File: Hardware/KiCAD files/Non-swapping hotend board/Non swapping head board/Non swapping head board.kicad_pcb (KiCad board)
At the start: 2 copper layers, 21.6 x 31.7 mm, 4 parts, among them J1 JST_06, J18 JST_1mm_3_Vertical, J20 PINHD_1x10_Female, J22 Conn_01x02

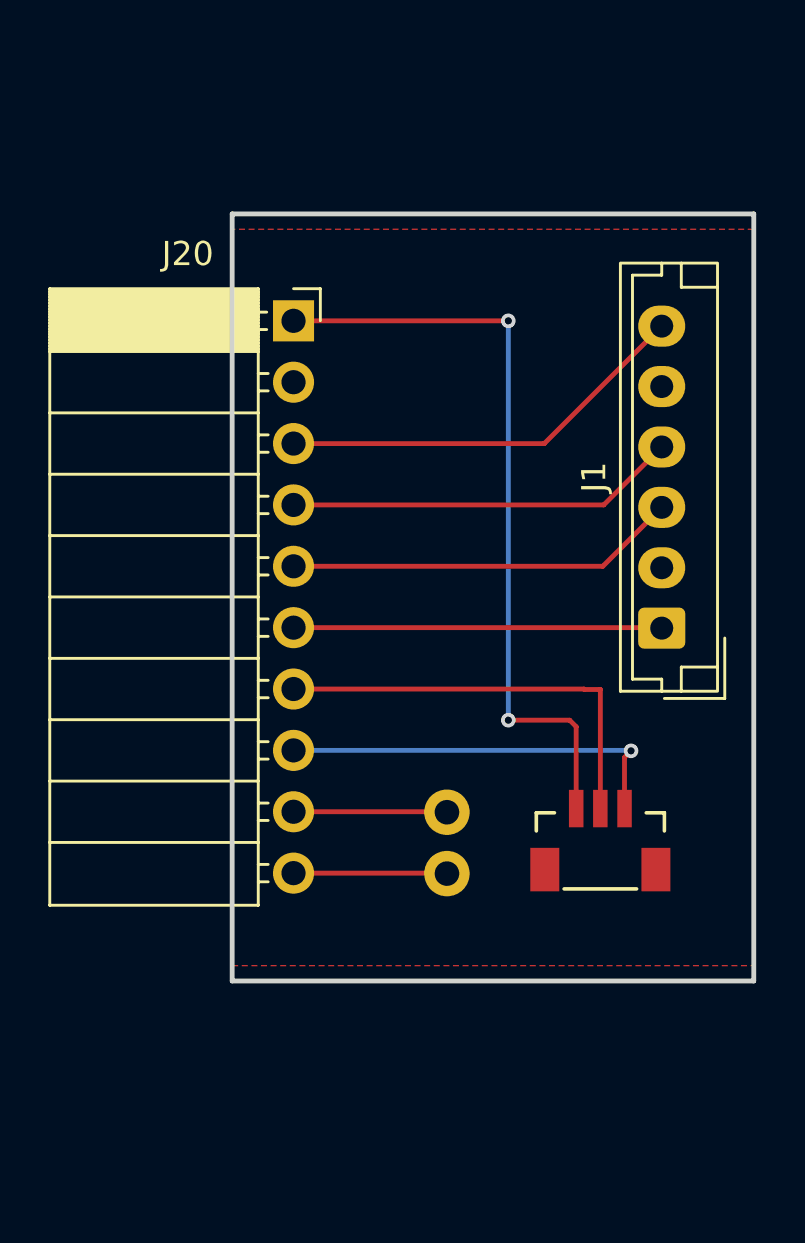
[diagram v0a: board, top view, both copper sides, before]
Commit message: 1st push of PCB's for printing
This is pre-peer review. This almost certainly has section that need adjustment. also realized I'm missing the USB-Uart bridge. first thing added in next version.
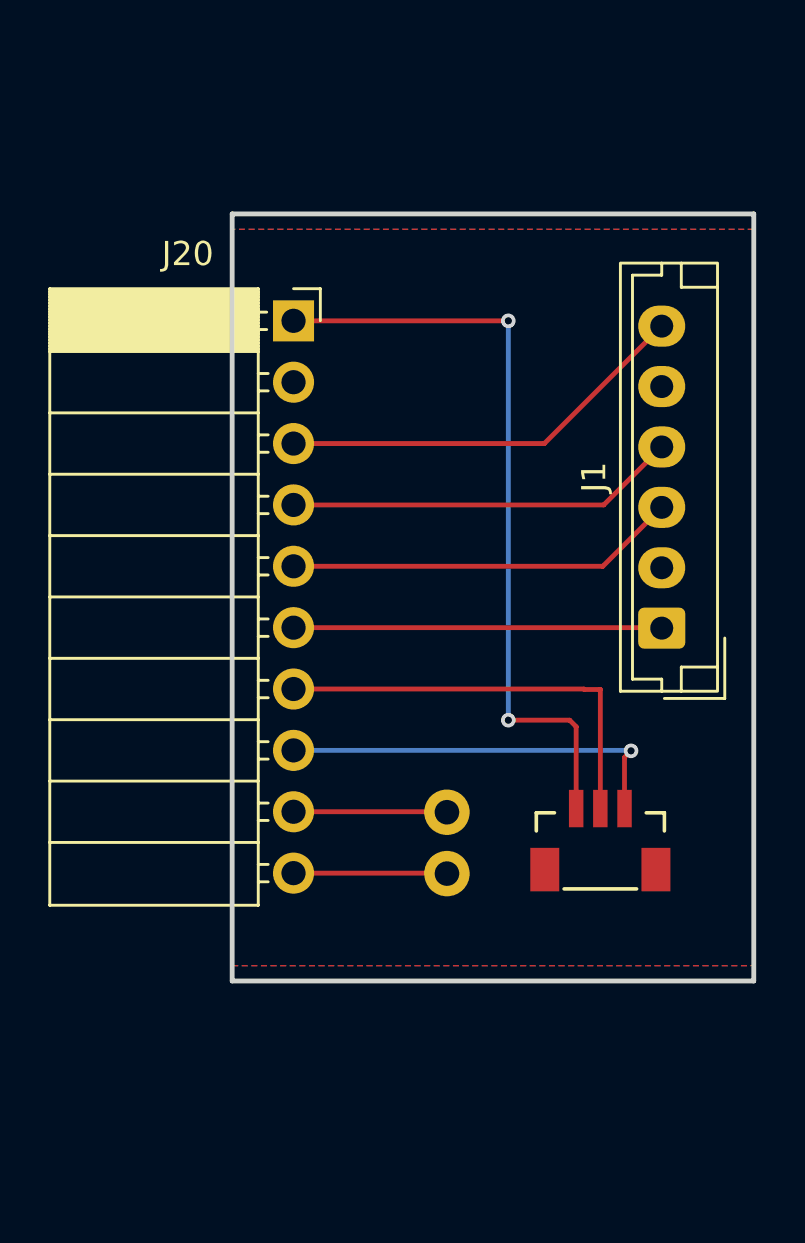
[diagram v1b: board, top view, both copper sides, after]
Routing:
- added copper zone on B.Cu, net GND
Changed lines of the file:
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@@
+	)
+	(segment
+		(start 109.49 61.23)
+		(end 109.22 60.96)
+		(width 0.2)
+		(layer "F.Cu")
+		(net "Net-(J18-Pad3)")
+	)
+	(segment
+		(start 109.22 60.96)
+		(end 106.68 60.96)
+		(width 0.2)
+		(layer "F.Cu")
+		(net "Net-(J18-Pad3)")
+	)
+	(segment
+		(start 106.68 44.43)
+		(end 97.79 44.43)
+		(width 0.2)
+		(layer "F.Cu")
+		(net "Net-(J18-Pad3)")
+	)
+	(segment
+		(start 109.49 64.6185)
+		(end 109.49 61.23)
+		(width 0.2)
+		(layer "F.Cu")
+		(net "Net-(J18-Pad3)")
+	)
+	(via
+		(at 106.68 60.96)
+		(size 0.6)
+		(drill 0.3)
+		(layers "F.Cu" "B.Cu")
+		(net "Net-(J18-Pad3)")
+	)
+	(via
+		(at 106.68 44.43)
+		(size 0.6)
+		(drill 0.3)
+		(layers "F.Cu" "B.Cu")
+		(net "Net-(J18-Pad3)")
+	)
+	(segment
+		(start 106.68 44.43)
+		(end 106.68 60.96)
+		(width 0.2)
+		(layer "B.Cu")
+		(net "Net-(J18-Pad3)")
+	)
+	(segment
+		(start 108.17 49.51)
+		(end 97.79 49.51)
+		(width 0.2)
+		(layer "F.Cu")
+		(net "/A1")
+	)
+	(segment
+		(start 113.03 44.65)
+		(end 108.17 49.51)
+		(width 0.2)
+		(layer "F.Cu")
+		(net "/A1")
+	)
+	(segment
+		(start 113.03 49.65)
+		(end 110.63 52.05)
+		(width 0.2)
+		(layer "F.Cu")
+		(net "/B1")
+	)
+	(segment
+		(start 110.63 52.05)
+		(end 97.79 52.05)
+		(width 0.2)
+		(layer "F.Cu")
+		(net "/B1")
+	)
+	(segment
+		(start 110.59 54.59)
+		(end 97.79 54.59)
+		(width 0.2)
+		(layer "F.Cu")
+		(net "/A2")
+	)
+	(segment
+		(start 113.03 52.15)
+		(end 110.59 54.59)
+		(width 0.2)
+		(layer "F.Cu")
+		(net "/A2")
+	)
+	(segment
+		(start 113.01 57.13)
+		(end 97.79 57.13)
+		(width 0.2)
+		(layer "F.Cu")
+		(net "/B2")
+	)
+	(segment
+		(start 113.03 57.15)
+		(end 113.01 57.13)
+		(width 0.2)
+		(layer "F.Cu")
+		(net "/B2")
+	)
+	(segment
+		(start 110.49 59.69)
+		(end 109.83 59.69)
+		(width 0.2)
+		(layer "F.Cu")
+		(net "Net-(J18-Pad2)")
+	)
+	(segment
+		(start 109.83 59.69)
+		(end 109.81 59.67)
+		(width 0.2)
+		(layer "F.Cu")
+		(net "Net-(J18-Pad2)")
+	)
+	(segment
+		(start 109.81 59.67)
+		(end 97.79 59.67)
+		(width 0.2)
+		(layer "F.Cu")
+		(net "Net-(J18-Pad2)")
+	)
+	(segment
+		(start 110.49 64.6185)
+		(end 110.49 59.69)
+		(width 0.2)
+		(layer "F.Cu")
+		(net "Net-(J18-Pad2)")
 	)
 	(segment
@@
 	)
 	(segment
-		(start 109.49 61.23)
-		(end 109.22 60.96)
-		(width 0.2)
-		(layer "F.Cu")
-		(net "Net-(J18-Pad3)")
-	)
-	(segment
-		(start 109.22 60.96)
-		(end 106.68 60.96)
-		(width 0.2)
-		(layer "F.Cu")
-		(net "Net-(J18-Pad3)")
-	)
-	(segment
-		(start 106.68 44.43)
-		(end 97.79 44.43)
-		(width 0.2)
-		(layer "F.Cu")
-		(net "Net-(J18-Pad3)")
-	)
-	(segment
-		(start 109.49 64.6185)
-		(end 109.49 61.23)
-		(width 0.2)
-		(layer "F.Cu")
-		(net "Net-(J18-Pad3)")
-	)
-	(via
-		(at 106.68 60.96)
-		(size 0.6)
-		(drill 0.3)
-		(layers "F.Cu" "B.Cu")
-		(net "Net-(J18-Pad3)")
-	)
-	(via
-		(at 106.68 44.43)
-		(size 0.6)
-		(drill 0.3)
-		(layers "F.Cu" "B.Cu")
-		(net "Net-(J18-Pad3)")
-	)
-	(segment
-		(start 106.68 44.43)
-		(end 106.68 60.96)
-		(width 0.2)
-		(layer "B.Cu")
-		(net "Net-(J18-Pad3)")
-	)
-	(segment
-		(start 110.49 59.69)
-		(end 109.83 59.69)
-		(width 0.2)
-		(layer "F.Cu")
-		(net "Net-(J18-Pad2)")
-	)
-	(segment
-		(start 109.83 59.69)
-		(end 109.81 59.67)
-		(width 0.2)
-		(layer "F.Cu")
-		(net "Net-(J18-Pad2)")
-	)
-	(segment
-		(start 109.81 59.67)
-		(end 97.79 59.67)
-		(width 0.2)
-		(layer "F.Cu")
-		(net "Net-(J18-Pad2)")
-	)
-	(segment
-		(start 110.49 64.6185)
-		(end 110.49 59.69)
-		(width 0.2)
-		(layer "F.Cu")
-		(net "Net-(J18-Pad2)")
-	)
-	(segment
 		(start 104.14 64.77)
 		(end 104.12 64.75)
@@
 		(net "Net-(J22-Pin_1)")
 	)
-	(segment
-		(start 113.01 57.13)
-		(end 97.79 57.13)
-		(width 0.2)
-		(layer "F.Cu")
-		(net "/B2")
-	)
-	(segment
-		(start 113.03 57.15)
-		(end 113.01 57.13)
-		(width 0.2)
-		(layer "F.Cu")
-		(net "/B2")
-	)
-	(segment
-		(start 108.17 49.51)
-		(end 97.79 49.51)
-		(width 0.2)
-		(layer "F.Cu")
-		(net "/A1")
-	)
-	(segment
-		(start 113.03 44.65)
-		(end 108.17 49.51)
-		(width 0.2)
-		(layer "F.Cu")
-		(net "/A1")
-	)
-	(segment
-		(start 110.59 54.59)
-		(end 97.79 54.59)
-		(width 0.2)
-		(layer "F.Cu")
-		(net "/A2")
-	)
-	(segment
-		(start 113.03 52.15)
-		(end 110.59 54.59)
-		(width 0.2)
-		(layer "F.Cu")
-		(net "/A2")
-	)
-	(segment
-		(start 113.03 49.65)
-		(end 110.63 52.05)
-		(width 0.2)
-		(layer "F.Cu")
-		(net "/B1")
-	)
-	(segment
-		(start 110.63 52.05)
-		(end 97.79 52.05)
-		(width 0.2)
-		(layer "F.Cu")
-		(net "/B1")
-	)
 	(zone
 		(net "GND")
-		(layer "F.Cu")
+		(layers "F.Cu" "B.Cu")
 		(name "GND")
 		(hatch edge 0.5)

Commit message: part of the way through next iteration
Non-daisy chain Mainboard is ~50% through
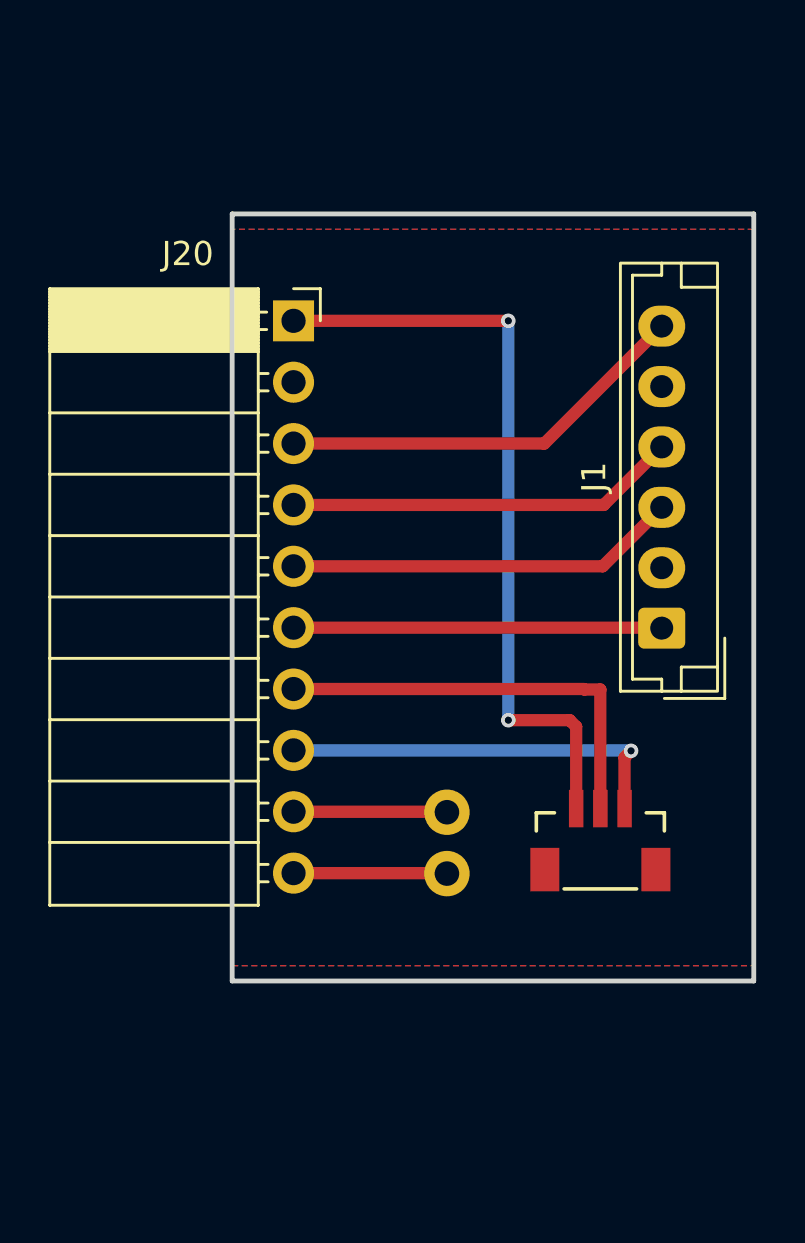
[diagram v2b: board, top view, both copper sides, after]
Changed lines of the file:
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@@
 		(start 109.49 61.23)
 		(end 109.22 60.96)
-		(width 0.2)
+		(width 0.508)
 		(layer "F.Cu")
 		(net "Net-(J18-Pad3)")
@@
 		(start 109.22 60.96)
 		(end 106.68 60.96)
-		(width 0.2)
+		(width 0.508)
 		(layer "F.Cu")
 		(net "Net-(J18-Pad3)")
@@
 		(start 106.68 44.43)
 		(end 97.79 44.43)
-		(width 0.2)
+		(width 0.508)
 		(layer "F.Cu")
 		(net "Net-(J18-Pad3)")
@@
 		(start 109.49 64.6185)
 		(end 109.49 61.23)
-		(width 0.2)
+		(width 0.508)
 		(layer "F.Cu")
 		(net "Net-(J18-Pad3)")
@@
 		(start 106.68 44.43)
 		(end 106.68 60.96)
-		(width 0.2)
+		(width 0.508)
 		(layer "B.Cu")
 		(net "Net-(J18-Pad3)")
@@
 		(start 108.17 49.51)
 		(end 97.79 49.51)
-		(width 0.2)
+		(width 0.508)
 		(layer "F.Cu")
 		(net "/A1")
@@
 		(start 113.03 44.65)
 		(end 108.17 49.51)
-		(width 0.2)
+		(width 0.508)
 		(layer "F.Cu")
 		(net "/A1")
@@
 		(start 113.03 49.65)
 		(end 110.63 52.05)
-		(width 0.2)
+		(width 0.508)
 		(layer "F.Cu")
 		(net "/B1")
@@
 		(start 110.63 52.05)
 		(end 97.79 52.05)
-		(width 0.2)
+		(width 0.508)
 		(layer "F.Cu")
 		(net "/B1")
@@
 		(start 110.59 54.59)
 		(end 97.79 54.59)
-		(width 0.2)
+		(width 0.508)
 		(layer "F.Cu")
 		(net "/A2")
@@
 		(start 113.03 52.15)
 		(end 110.59 54.59)
-		(width 0.2)
+		(width 0.508)
 		(layer "F.Cu")
 		(net "/A2")
@@
 		(start 113.01 57.13)
 		(end 97.79 57.13)
-		(width 0.2)
+		(width 0.508)
 		(layer "F.Cu")
 		(net "/B2")
@@
 		(start 113.03 57.15)
 		(end 113.01 57.13)
-		(width 0.2)
+		(width 0.508)
 		(layer "F.Cu")
 		(net "/B2")
@@
 		(start 110.49 59.69)
 		(end 109.83 59.69)
-		(width 0.2)
+		(width 0.508)
 		(layer "F.Cu")
 		(net "Net-(J18-Pad2)")
@@
 		(start 109.83 59.69)
 		(end 109.81 59.67)
-		(width 0.2)
+		(width 0.508)
 		(layer "F.Cu")
 		(net "Net-(J18-Pad2)")
@@
 		(start 109.81 59.67)
 		(end 97.79 59.67)
-		(width 0.2)
+		(width 0.508)
 		(layer "F.Cu")
 		(net "Net-(J18-Pad2)")
@@
 		(start 110.49 64.6185)
 		(end 110.49 59.69)
-		(width 0.2)
+		(width 0.508)
 		(layer "F.Cu")
 		(net "Net-(J18-Pad2)")
@@
 		(start 111.49 64.6185)
 		(end 111.49 62.5)
-		(width 0.2)
+		(width 0.508)
 		(layer "F.Cu")
 		(net "Net-(J18-Pad1)")
@@
 		(start 111.49 62.5)
 		(end 111.76 62.23)
-		(width 0.2)
+		(width 0.508)
 		(layer "F.Cu")
 		(net "Net-(J18-Pad1)")
@@
 		(start 111.74 62.21)
 		(end 97.79 62.21)
-		(width 0.2)
+		(width 0.508)
 		(layer "B.Cu")
 		(net "Net-(J18-Pad1)")
@@
 		(start 111.76 62.23)
 		(end 111.74 62.21)
-		(width 0.2)
+		(width 0.508)
 		(layer "B.Cu")
 		(net "Net-(J18-Pad1)")
@@
 		(start 104.14 64.77)
 		(end 104.12 64.75)
-		(width 0.2)
+		(width 0.508)
 		(layer "F.Cu")
 		(net "Net-(J22-Pin_2)")
@@
 		(start 104.12 64.75)
 		(end 97.79 64.75)
-		(width 0.2)
+		(width 0.508)
 		(layer "F.Cu")
 		(net "Net-(J22-Pin_2)")
@@
 		(start 104.14 67.31)
 		(end 104.12 67.29)
-		(width 0.2)
+		(width 0.508)
 		(layer "F.Cu")
 		(net "Net-(J22-Pin_1)")
@@
 		(start 104.12 67.29)
 		(end 97.79 67.29)
-		(width 0.2)
+		(width 0.508)
 		(layer "F.Cu")
 		(net "Net-(J22-Pin_1)")
